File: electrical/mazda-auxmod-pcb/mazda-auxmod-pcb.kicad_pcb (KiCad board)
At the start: 2 copper layers, 80.8 x 27.7 mm, 33 parts, among them J1 Conn_01x15_Shielded, J2 Conn_01x10, J3 AudioJack4_Ground, J4 Conn_01x03, Q1 2N3904, Q2 2N3904, Q3 2SA715, U1 ATtiny45-20P, U2 L78L05_TO92, U3 L7805

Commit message: neatened up schematic/pcb
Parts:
- J3: footprint Connector_Audio:Jack_3.5mm_PJ320E_Horizontal -> Connector_Audio:Jack_3.5mm_PJ320D_Horizontal
- moved J3 4.26 mm to (210.0, 58.4), turned to 180 degrees
- moved R16 3.70 mm to (213.1, 72.1)
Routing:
- net Net-(J3-PadR1): track 5.82 -> 12.5 mm
- net Net-(J3-PadT): track 10.4 -> 16.4 mm
- net /iPod Acc Input: track 3.81 -> 7.79 mm
- net GND: vias 33 -> 34

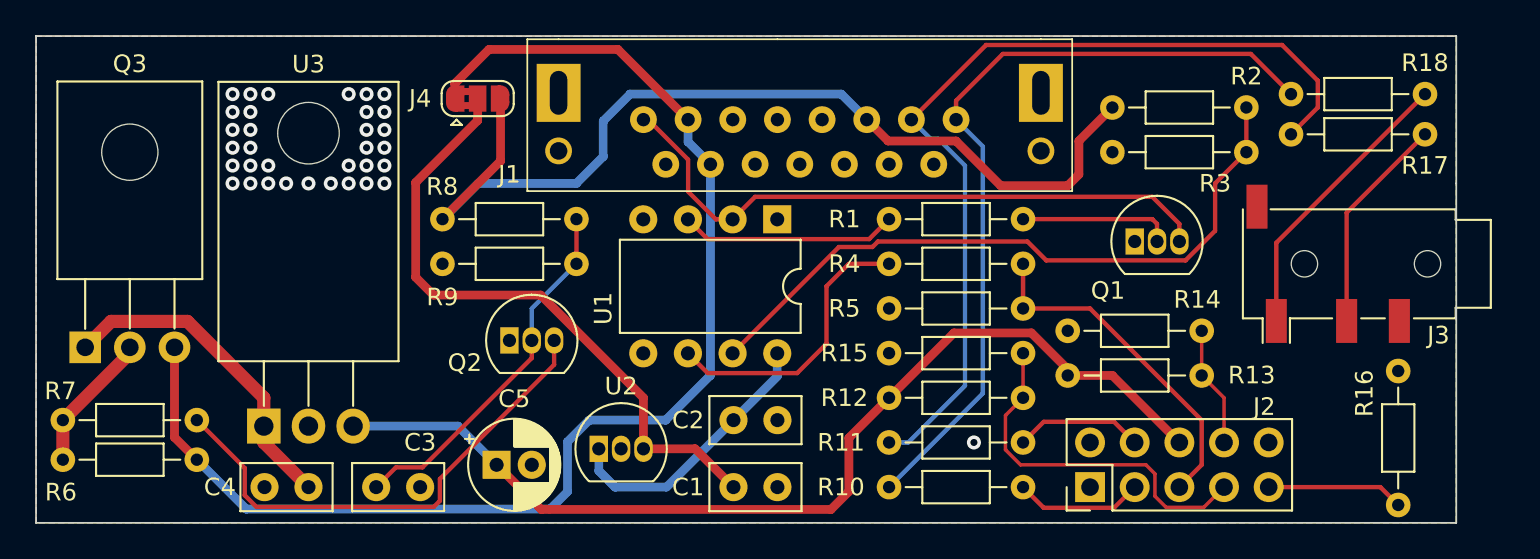
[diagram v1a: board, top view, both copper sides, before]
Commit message: fixed footprint for radio connector
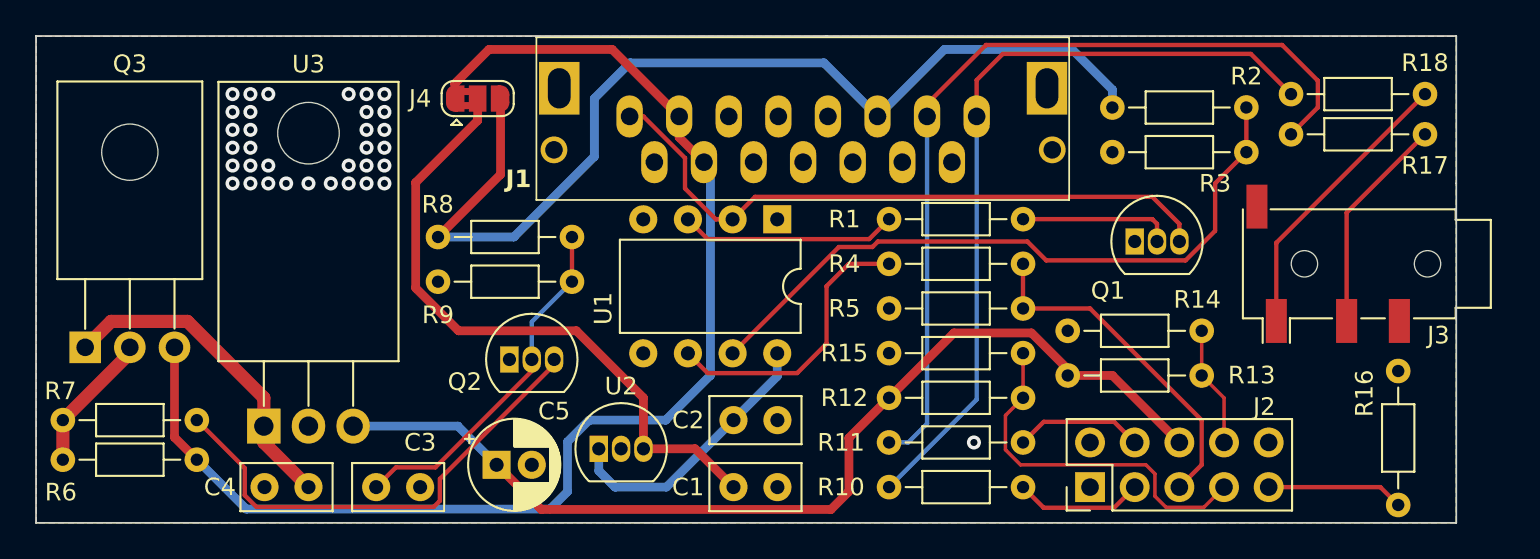
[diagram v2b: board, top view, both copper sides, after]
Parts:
- moved Q2 1.08 mm to (162.6, 63.9)
- moved R8 1.05 mm to (158.5, 56.9)
- moved R9 1.05 mm to (166.1, 59.4)
- moved J1 0.81 mm to (169.4, 50.0)
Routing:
- net +12V: track 55.6 -> 58.5 mm
- net /Audio Right: track 51.7 -> 48.9 mm
- net /Audio Left: track 45.9 -> 44.7 mm
- net Net-(Q2-C): track 28.7 -> 27.7 mm
- net /Radio Bus: track 36.1 -> 36.9 mm
- net Net-(Q2-B): track 20.8 -> 20.2 mm

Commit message: added version info to pcb
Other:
- board text added: "Mazda AuxMod v1.0.1"
- board text added: "github.com/andrewandneil/mazda-auxmod"
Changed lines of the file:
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@@
   (gr_line (start 216.408 53.848) (end 216.408 45.466)
     (stroke (width 0.1) (type default)) (layer "Edge.Cuts"))
+  (gr_text "Mazda AuxMod\nv1.0.1" (at 181.61 60.198) (layer "B.SilkS")
+    (effects (font (size 1 1) (thickness 0.2) bold) (justify left bottom mirror))
+  )
+  (gr_text "github.com/andrewandneil/mazda-auxmod\n" (at 181.864 61.976) (layer "B.SilkS")
+    (effects (font (size 1 1) (thickness 0.2) bold) (justify left bottom mirror))
+  )
   (segment (start 161.396 46.228) (end 168.402 46.228) (width 0.5) (layer "F.Cu") (net 1))
   (segment (start 168.402 46.228) (end 172.212 50.038) (width 0.5) (layer "F.Cu") (net 1))
